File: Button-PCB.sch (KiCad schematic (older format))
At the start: 32 parts

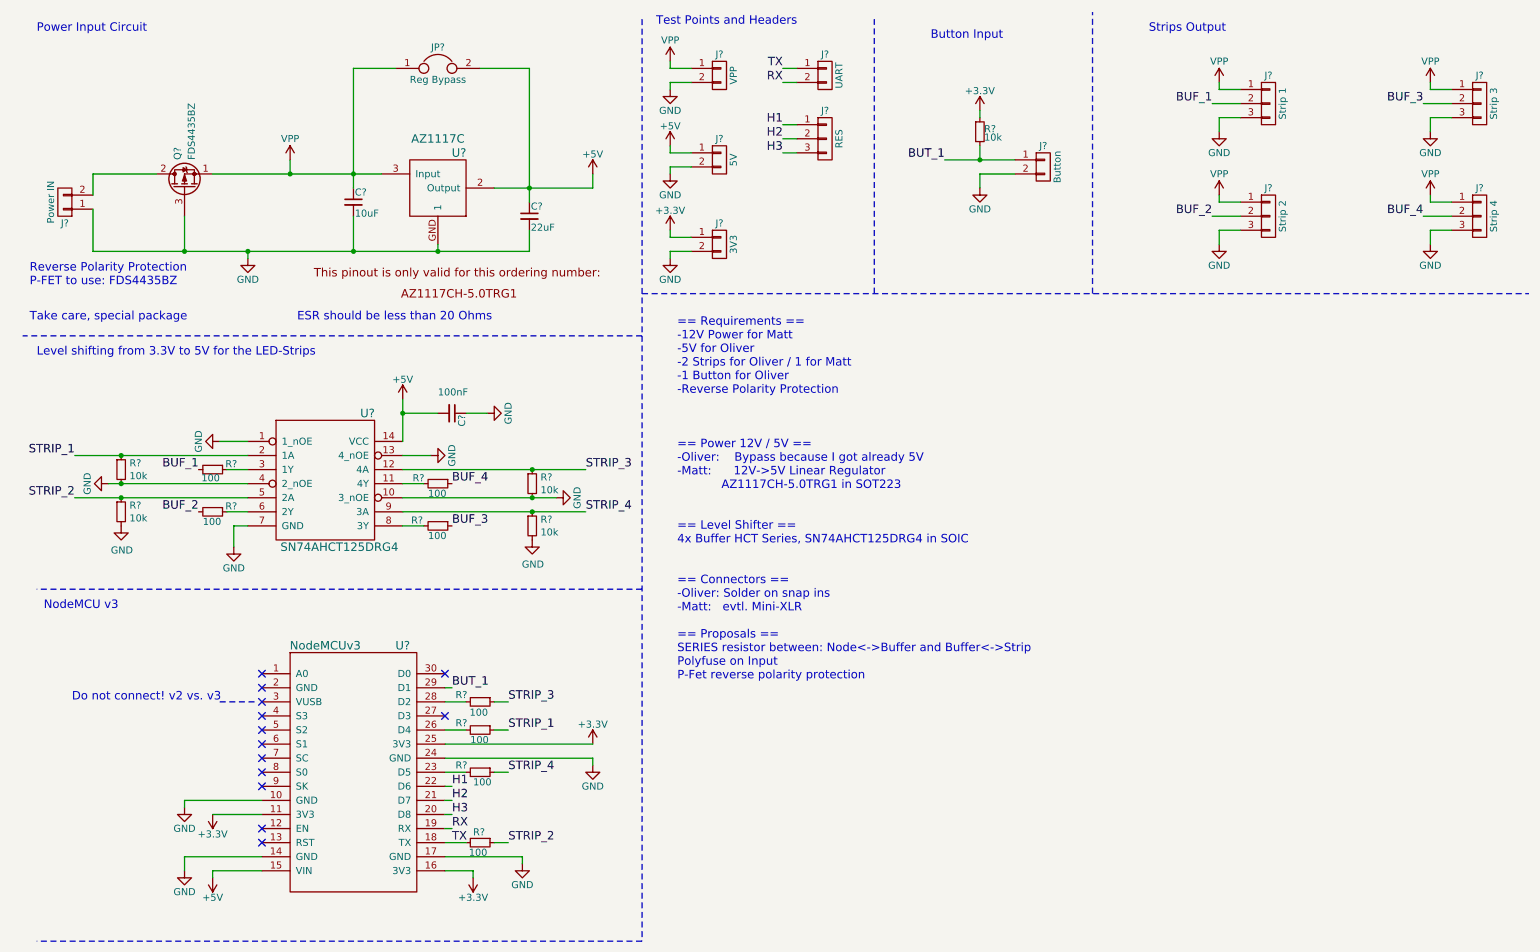
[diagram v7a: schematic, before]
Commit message: Minor schematic rework to tie up loose ends. No functional changes.
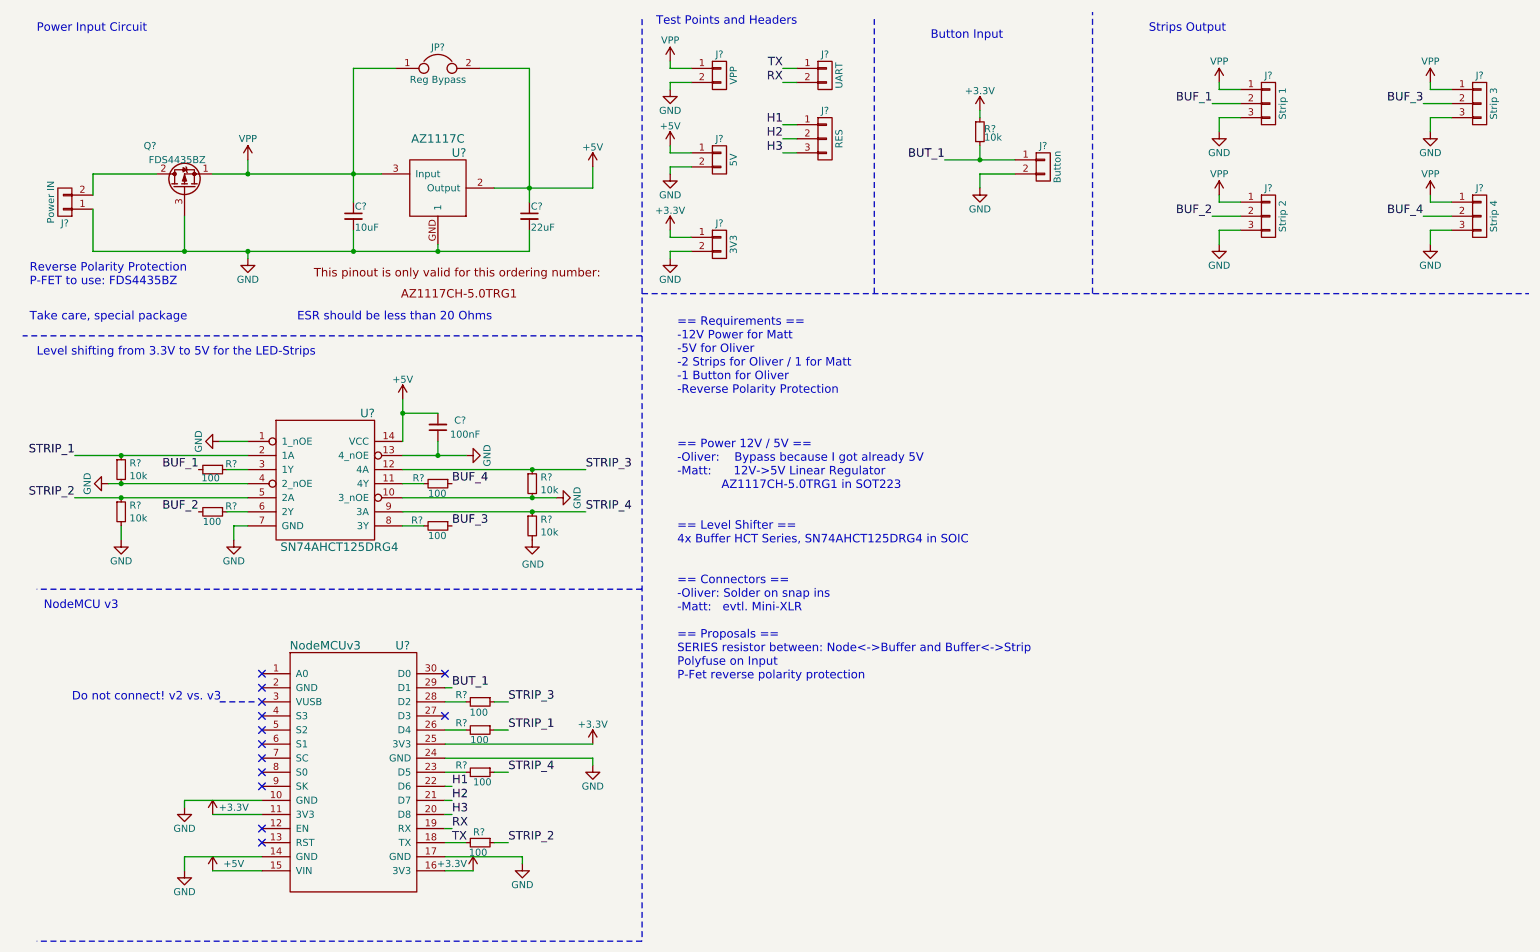
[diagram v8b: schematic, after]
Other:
- moved on the sheet: C?
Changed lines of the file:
@@
 	7300 1250 7300 1200
 Wire Wire Line
-	7050 1550 7300 1550
-Wire Wire Line
-	7300 1550 7550 1550
+	7050 1550 7550 1550
 Wire Wire Line
 	7300 1550 7300 1450
@@
 L +3.3V #PWR?
 U 1 1 593F10EA
-P 3700 6650
-F 0 "#PWR?" H 3700 6500 50  0001 C CNN
-F 1 "+3.3V" H 3700 6790 50  0000 C CNN
-F 2 "" H 3700 6650 50  0001 C CNN
-F 3 "" H 3700 6650 50  0001 C CNN
-	1    3700 6650
-	-1   0    0    1
+P 3700 6600
+F 0 "#PWR?" H 3700 6450 50  0001 C CNN
+F 1 "+3.3V" H 3550 6650 50  0000 C CNN
+F 2 "" H 3700 6600 50  0001 C CNN
+F 3 "" H 3700 6600 50  0001 C CNN
+	1    3700 6600
+	1    0    0    -1
 $EndComp
 $Comp
@@
 P 1850 6200
 F 0 "#PWR?" H 1850 6050 50  0001 C CNN
-F 1 "+3.3V" H 1850 6340 50  0000 C CNN
+F 1 "+3.3V" H 2000 6250 50  0000 C CNN
 F 2 "" H 1850 6200 50  0001 C CNN
 F 3 "" H 1850 6200 50  0001 C CNN
 	1    1850 6200
-	-1   0    0    1
+	1    0    0    -1
 $EndComp
 Wire Wire Line
@@
 Wire Wire Line
 	3500 6600 3700 6600
-Wire Wire Line
-	3700 6600 3700 6650
 Wire Wire Line
 	3500 5700 4550 5700
@@
 L +5V #PWR?
 U 1 1 593F22C9
-P 1850 6650
-F 0 "#PWR?" H 1850 6500 50  0001 C CNN
-F 1 "+5V" H 1850 6790 50  0000 C CNN
-F 2 "" H 1850 6650 50  0001 C CNN
-F 3 "" H 1850 6650 50  0001 C CNN
-	1    1850 6650
-	-1   0    0    1
-$EndComp
-Wire Wire Line
-	1850 6650 1850 6600
+P 1850 6600
+F 0 "#PWR?" H 1850 6450 50  0001 C CNN
+F 1 "+5V" H 2000 6650 50  0000 C CNN
+F 2 "" H 1850 6600 50  0001 C CNN
+F 3 "" H 1850 6600 50  0001 C CNN
+	1    1850 6600
+	1    0    0    -1
+$EndComp
 Wire Wire Line
 	1850 6600 2200 6600
@@
 L +5V #PWR?
 U 1 1 593F7638
-P 4550 1650
-F 0 "#PWR?" H 4550 1500 50  0001 C CNN
-F 1 "+5V" H 4550 1790 50  0000 C CNN
-F 2 "" H 4550 1650 50  0001 C CNN
-F 3 "" H 4550 1650 50  0001 C CNN
-	1    4550 1650
+P 4550 1600
+F 0 "#PWR?" H 4550 1450 50  0001 C CNN
+F 1 "+5V" H 4550 1740 50  0000 C CNN
+F 2 "" H 4550 1600 50  0001 C CNN
+F 3 "" H 4550 1600 50  0001 C CNN
+	1    4550 1600
 	1    0    0    -1
 $EndComp
@@
 L C_Small C?
 U 1 1 593F77E1
-P 2850 1850
-F 0 "C?" H 2860 1920 50  0000 L CNN
-F 1 "10uF" H 2860 1770 50  0000 L CNN
-F 2 "" H 2850 1850 50  0001 C CNN
-F 3 "" H 2850 1850 50  0001 C CNN
-	1    2850 1850
+P 2850 1950
+F 0 "C?" H 2860 2020 50  0000 L CNN
+F 1 "10uF" H 2860 1870 50  0000 L CNN
+F 2 "" H 2850 1950 50  0001 C CNN
+F 3 "" H 2850 1950 50  0001 C CNN
+	1    2850 1950
 	1    0    0    -1
 $EndComp
@@
 	3450 2200 3450 2150
 Wire Wire Line
-	3850 1750 4100 1750
-Wire Wire Line
-	4100 1750 4550 1750
-Wire Wire Line
-	4550 1750 4550 1650
-Wire Wire Line
-	4100 900  4100 1750
-Wire Wire Line
-	4100 1750 4100 1850
+	3850 1750 4550 1750
+Wire Wire Line
+	4550 1750 4550 1600
+Wire Wire Line
+	4100 900  4100 1850
 Connection ~ 4100 1750
 Wire Wire Line
-	1000 2200 1650 2200
-Wire Wire Line
-	1650 2200 2100 2200
-Wire Wire Line
-	2100 2200 2850 2200
-Wire Wire Line
-	2850 2200 3450 2200
-Wire Wire Line
-	3450 2200 4100 2200
+	1000 2200 4100 2200
 Connection ~ 3450 2200
 Wire Wire Line
-	2850 1950 2850 2200
+	2850 2050 2850 2200
 Connection ~ 2850 2200
 Wire Wire Line
-	2850 900  2850 1650
-Wire Wire Line
-	2850 1650 2850 1750
-Wire Wire Line
-	1850 1650 2400 1650
-Wire Wire Line
-	2400 1650 2850 1650
-Wire Wire Line
-	2850 1650 3050 1650
+	2850 900  2850 1850
+Wire Wire Line
+	1850 1650 3050 1650
 $Comp
 L Jumper JP?
@@
 L VPP #PWR?
 U 1 1 593F9797
-P 2400 1550
-F 0 "#PWR?" H 2400 1400 50  0001 C CNN
-F 1 "VPP" H 2400 1700 50  0000 C CNN
-F 2 "" H 2400 1550 50  0001 C CNN
-F 3 "" H 2400 1550 50  0001 C CNN
-	1    2400 1550
-	1    0    0    -1
-$EndComp
-Wire Wire Line
-	2400 1550 2400 1650
+P 2100 1550
+F 0 "#PWR?" H 2100 1400 50  0001 C CNN
+F 1 "VPP" H 2100 1700 50  0000 C CNN
+F 2 "" H 2100 1550 50  0001 C CNN
+F 3 "" H 2100 1550 50  0001 C CNN
+	1    2100 1550
+	1    0    0    -1
+$EndComp
+Wire Wire Line
+	2100 1550 2100 1650
 Text Notes 600  650  0    60   ~ 0
 Power Input Circuit
@@
 U 1 1 5942ACB6
 P 1650 1750
-F 0 "Q?" H 1850 1800 50  0000 L CNN
-F 1 "FDS4435BZ" H 1850 1700 50  0000 L CNN
+F 0 "Q?" V 1950 1950 50  0000 L CNN
+F 1 "FDS4435BZ" V 1850 1600 50  0000 L CNN
 F 2 "" H 1850 1850 50  0001 C CNN
 F 3 "" H 1650 1750 50  0001 C CNN
@@
 	1000 1900 1000 2200
 Connection ~ 2100 2200
-Connection ~ 2400 1650
+Connection ~ 2100 1650
 Wire Wire Line
 	1450 1650 1000 1650
@@
 L GND #PWR?
 U 1 1 5942C149
-P 2000 4300
-F 0 "#PWR?" H 2000 4050 50  0001 C CNN
-F 1 "GND" H 2000 4150 50  0000 C CNN
-F 2 "" H 2000 4300 50  0001 C CNN
-F 3 "" H 2000 4300 50  0001 C CNN
-	1    2000 4300
+P 2000 4250
+F 0 "#PWR?" H 2000 4000 50  0001 C CNN
+F 1 "GND" H 2000 4100 50  0000 C CNN
+F 2 "" H 2000 4250 50  0001 C CNN
+F 3 "" H 2000 4250 50  0001 C CNN
+	1    2000 4250
 	1    0    0    -1
 $EndComp
@@
 L GND #PWR?
 U 1 1 5942C449
-P 3400 3650
-F 0 "#PWR?" H 3400 3400 50  0001 C CNN
-F 1 "GND" H 3400 3500 50  0000 C CNN
-F 2 "" H 3400 3650 50  0001 C CNN
-F 3 "" H 3400 3650 50  0001 C CNN
-	1    3400 3650
+P 3650 3650
+F 0 "#PWR?" H 3650 3400 50  0001 C CNN
+F 1 "GND" H 3650 3500 50  0000 C CNN
+F 2 "" H 3650 3650 50  0001 C CNN
+F 3 "" H 3650 3650 50  0001 C CNN
+	1    3650 3650
 	0    -1   -1   0
 $EndComp
@@
 	2000 4150 2100 4150
 Wire Wire Line
-	2000 4300 2000 4150
+	2000 4250 2000 4150
 Wire Wire Line
 	1950 3750 2100 3750
 Wire Wire Line
-	870  3650 1200 3650
-Wire Wire Line
-	1200 3650 2100 3650
-Wire Wire Line
-	870  3950 1200 3950
-Wire Wire Line
-	1200 3950 2100 3950
+	870  3650 2100 3650
+Wire Wire Line
+	870  3950 2100 3950
 $Comp
 L GND #PWR?
@@
 $EndComp
 Wire Wire Line
-	1110 3850 1200 3850
-Wire Wire Line
-	1200 3850 2100 3850
+	1110 3850 2100 3850
 $Comp
 L GND #PWR?
@@
 	1900 3550 2100 3550
 Wire Wire Line
-	3200 3950 4120 3950
-Wire Wire Line
-	4120 3950 4290 3950
-Wire Wire Line
-	3400 3650 3200 3650
+	3200 3950 4290 3950
+Wire Wire Line
+	3200 3650 3650 3650
 $Comp
 L R_Small R?
@@
 $EndComp
 Wire Wire Line
-	3200 3750 4120 3750
-Wire Wire Line
-	4120 3750 4500 3750
-Wire Wire Line
-	3200 4050 4120 4050
-Wire Wire Line
-	4120 4050 4500 4050
+	3200 3750 4500 3750
+Wire Wire Line
+	3200 4050 4500 4050
 $Comp
 L C_Small C?
 U 1 1 5942F9D6
-P 3550 3350
-F 0 "C?" H 3560 3420 50  0000 L CNN
-F 1 "100nF" V 3400 3250 50  0000 L CNN
-F 2 "" H 3550 3350 50  0001 C CNN
-F 3 "" H 3550 3350 50  0001 C CNN
-	1    3550 3350
-	0    1    1    0
-$EndComp
-$Comp
-L GND #PWR?
-U 1 1 5942FB69
-P 3800 3350
-F 0 "#PWR?" H 3800 3100 50  0001 C CNN
-F 1 "GND" H 3800 3200 50  0000 C CNN
-F 2 "" H 3800 3350 50  0001 C CNN
-F 3 "" H 3800 3350 50  0001 C CNN
-	1    3800 3350
-	0    -1   -1   0
-$EndComp
-Wire Wire Line
-	3800 3350 3650 3350
+P 3450 3450
+F 0 "C?" H 3250 3400 50  0000 L CNN
+F 1 "100nF" H 3150 3500 50  0000 L CNN
+F 2 "" H 3450 3450 50  0001 C CNN
+F 3 "" H 3450 3450 50  0001 C CNN
+	1    3450 3450
+	-1   0    0    1
+$EndComp
 Wire Wire Line
 	3450 3350 3200 3350
 Wire Wire Line
-	3200 3250 3200 3350
-Wire Wire Line
-	3200 3350 3200 3550
+	3200 3250 3200 3550
 $Comp
 L +5V #PWR?
@@
 L GND #PWR?
 U 1 1 5945C779
-P 1200 4150
-F 0 "#PWR?" H 1200 3900 50  0001 C CNN
-F 1 "GND" H 1205 3977 50  0000 C CNN
-F 2 "" H 1200 4150 50  0001 C CNN
-F 3 "" H 1200 4150 50  0001 C CNN
-	1    1200 4150
+P 1200 4250
+F 0 "#PWR?" H 1200 4000 50  0001 C CNN
+F 1 "GND" H 1200 4100 50  0000 C CNN
+F 2 "" H 1200 4250 50  0001 C CNN
+F 3 "" H 1200 4250 50  0001 C CNN
+	1    1200 4250
 	1    0    0    -1
 $EndComp
@@
 Wire Wire Line
 	3950 5400 3850 5400
+Wire Wire Line
+	3450 3550 3450 3650
+Connection ~ 3450 3650
+Wire Wire Line
+	1200 4150 1200 4250
 $EndSCHEMATC
